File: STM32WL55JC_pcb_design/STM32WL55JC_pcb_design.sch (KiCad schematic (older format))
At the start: 27 parts

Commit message: Complete first version - todo: rf pins
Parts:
- removed J?: Conn_01x10_Male, Connector_JST:JST_GH_BM10B-GHS-TBT_1x10-1MP_P1.25mm_Vertical, symbol Connector:Conn_01x10_Male
- removed J?: Conn_01x07_Male, symbol Connector:Conn_01x07_Male
- added J?: Conn_02x02_Odd_Even, symbol Connector_Generic:Conn_02x02_Odd_Even
- added J?: Conn_01x06, symbol Connector_Generic:Conn_01x06
- added J?: Conn_02x05_Odd_Even, symbol Connector_Generic:Conn_02x05_Odd_Even
- added J?: Conn_01x13_Male, symbol Connector:Conn_01x13_Male
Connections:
- net labels added: 29V5, 5V, ADC_DO1, ADC_DO2, EXP_INT, EXP_SCL, EXP_SDA, NCS1_1, NCS1_2, NCS2_1, NCS2_2, NCS3_1, NCS3_2, NCS4_1, NCS4_2, NRST, OR1, OR2, OR3, OR4, PA0, PA1, PA7, PB0, PB1, PB10, PB11, PB6, PC0, PC1, PC4, PC5, PC6, SPI1_CLK, SPI2_CLK, SWCLK, SWDIO, SWO
- net labels removed: 29V, ADC1_CS, ADC2_CS, ADC_DOUT, ADC_SCLK, ENC1_1, ENC1_2, ENC1_3, ENC1_4, ENC2_1, ENC2_2, ENC2_3, ENC2_4, GND1, OR, Reset
- wire segments 151 -> 220
- no-connect marks 0 -> 2
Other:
- note added: "ST-Link Connector"
- note added: "Scintillator subsystem"

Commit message: Add temperature and humidty sensor, add rf connections
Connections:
- net labels added: PA8, RFI_N, RFI_P, RFO_HP, TempHumid_DRDY, VR_PA
- net labels removed: PB6, USB_RX, USB_TX
- wire segments 220 -> 227
- no-connect marks 2 -> 3
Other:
- moved on the sheet: J?
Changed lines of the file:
@@
 $Descr A4 11693 8268
 encoding utf-8
-Sheet 1 5
+Sheet 1 7
 Title ""
 Date ""
@@
 	1    0    0    -1
 $EndComp
-Text GLabel 8950 2400 2    50   Input ~ 0
+Text GLabel 8900 2400 2    50   Input ~ 0
 SPI1_CLK
 Wire Wire Line
@@
 	1    0    0    -1
 $EndComp
-$Sheet
-S 750  2100 750  1000
-U 612BE788
-F0 "Power Supply" 50
-F1 "Power supply.sch" 50
-F2 "3.3V" I R 1500 2300 50
-F3 "GND" I R 1500 2400 50
-F4 "USB_TX" I R 1500 2700 50
-F5 "USB_RX" I R 1500 2800 50
-F6 "29V5" I R 1500 2950 50
-F7 "5V" I R 1500 3050 50
-$EndSheet
 $Comp
 L power:+3.3V #PWR?
@@
 	1    0    0    -1
 $EndComp
-Text GLabel 3100 2350 2    50   Input ~ 0
+Text GLabel 3150 2450 2    50   Input ~ 0
 SCL
 Wire Wire Line
-	2950 2350 3100 2350
-$Sheet
-S 2150 2100 800  850
-U 61317136
-F0 "GPS and accelerometer" 50
-F1 "GPS_ACC.sch" 50
-F2 "SDA" I R 2950 2250 50
-F3 "SCL" I R 2950 2350 50
-F4 "TX" I R 2950 2500 50
-F5 "RX" I R 2950 2600 50
-$EndSheet
-Text GLabel 3100 2250 2    50   Input ~ 0
+	3000 2450 3150 2450
+Text GLabel 3150 2350 2    50   Input ~ 0
 SDA
 Wire Wire Line
-	2950 2250 3100 2250
+	3000 2350 3150 2350
 $Comp
 L STM32WL55JC_pcb_design-rescue:STM32WL55JCI7-MCU_ST_STM3255JCI7 U?
@@
 	1    0    0    -1
 $EndComp
-Text GLabel 3100 2600 2    50   Input ~ 0
+Text GLabel 3150 2700 2    50   Input ~ 0
 RX
 Wire Wire Line
-	2950 2600 3100 2600
-Wire Wire Line
-	2950 2500 3100 2500
-Text GLabel 3100 2500 2    50   Input ~ 0
+	3000 2700 3150 2700
+Wire Wire Line
+	3000 2600 3150 2600
+Text GLabel 3150 2600 2    50   Input ~ 0
 TX
 Wire Wire Line
-	1500 2700 1650 2700
-Wire Wire Line
-	1500 2800 1650 2800
-Text GLabel 1650 2800 2    50   Input ~ 0
-USB_RX
-Text GLabel 1650 2700 2    50   Input ~ 0
-USB_TX
-Wire Wire Line
 	4850 5000 4850 4900
 Wire Wire Line
-	4850 4900 4700 4900
-Wire Wire Line
-	4700 4900 4700 4950
+	4300 4900 4300 4950
 $Comp
 L power:GNDREF #PWR?
 U 1 1 61386153
-P 4700 4950
-F 0 "#PWR?" H 4700 4700 50  0001 C CNN
-F 1 "GNDREF" H 4705 4777 50  0000 C CNN
-F 2 "" H 4700 4950 50  0001 C CNN
-F 3 "" H 4700 4950 50  0001 C CNN
-	1    4700 4950
+P 4300 4950
+F 0 "#PWR?" H 4300 4700 50  0001 C CNN
+F 1 "GNDREF" H 4305 4777 50  0000 C CNN
+F 2 "" H 4300 4950 50  0001 C CNN
+F 3 "" H 4300 4950 50  0001 C CNN
+	1    4300 4950
 	1    0    0    -1
 $EndComp
@@
 	8750 3000 8900 3000
 Wire Wire Line
-	8750 2900 9000 2900
-Wire Wire Line
-	9000 2900 9000 2800
-Wire Wire Line
-	9350 2800 9350 2850
+	9250 2900 9250 2800
+Wire Wire Line
+	9600 2800 9600 2850
 $Comp
 L power:GNDREF #PWR?
 U 1 1 61439C4E
-P 9350 2850
-F 0 "#PWR?" H 9350 2600 50  0001 C CNN
-F 1 "GNDREF" H 9355 2677 50  0000 C CNN
-F 2 "" H 9350 2850 50  0001 C CNN
-F 3 "" H 9350 2850 50  0001 C CNN
-	1    9350 2850
-	1    0    0    -1
-$EndComp
-Wire Wire Line
-	9000 2800 9350 2800
+P 9600 2850
+F 0 "#PWR?" H 9600 2600 50  0001 C CNN
+F 1 "GNDREF" H 9605 2677 50  0000 C CNN
+F 2 "" H 9600 2850 50  0001 C CNN
+F 3 "" H 9600 2850 50  0001 C CNN
+	1    9600 2850
+	1    0    0    -1
+$EndComp
+Wire Wire Line
+	9250 2800 9600 2800
 $Comp
 L Device:C C?
@@
 Text GLabel 6850 900  1    50   Input ~ 0
 VDDPA
-Text GLabel 8950 2700 2    50   Input ~ 0
+Text GLabel 8900 2700 2    50   Input ~ 0
 VDDPA
 $Comp
@@
 Wire Wire Line
 	5200 3900 5350 3900
-Wire Wire Line
-	8750 2200 8950 2200
 $Comp
 L Connector_Generic:Conn_02x02_Odd_Even J?
 U 1 1 61363B01
-P 9150 2150
-F 0 "J?" H 9200 2367 50  0000 C CNN
-F 1 "Conn_02x02_Odd_Even" H 9200 2276 50  0000 C CNN
-F 2 "" H 9150 2150 50  0001 C CNN
-F 3 "~" H 9150 2150 50  0001 C CNN
-	1    9150 2150
-	1    0    0    -1
-$EndComp
-Wire Wire Line
-	8950 2200 8950 2150
-Wire Wire Line
-	8950 2200 8950 2250
-Connection ~ 8950 2200
-Wire Wire Line
-	9450 2150 9700 2150
-Wire Wire Line
-	9700 2150 9700 1950
+P 9500 2150
+F 0 "J?" H 9550 2367 50  0000 C CNN
+F 1 "Conn_02x02_Odd_Even" H 9550 2276 50  0000 C CNN
+F 2 "" H 9500 2150 50  0001 C CNN
+F 3 "~" H 9500 2150 50  0001 C CNN
+	1    9500 2150
+	1    0    0    -1
+$EndComp
+Wire Wire Line
+	9300 2200 9300 2150
+Wire Wire Line
+	9300 2200 9300 2250
+Connection ~ 9300 2200
+Wire Wire Line
+	9800 2150 10050 2150
+Wire Wire Line
+	10050 2150 10050 1950
 $Comp
 L power:+3.3V #PWR?
 U 1 1 6137A2D6
-P 9700 1950
-F 0 "#PWR?" H 9700 1800 50  0001 C CNN
-F 1 "+3.3V" H 9715 2123 50  0000 C CNN
-F 2 "" H 9700 1950 50  0001 C CNN
-F 3 "" H 9700 1950 50  0001 C CNN
-	1    9700 1950
-	1    0    0    -1
-$EndComp
-Wire Wire Line
-	9450 2250 9700 2250
-Wire Wire Line
-	9700 2250 9700 2450
+P 10050 1950
+F 0 "#PWR?" H 10050 1800 50  0001 C CNN
+F 1 "+3.3V" H 10065 2123 50  0000 C CNN
+F 2 "" H 10050 1950 50  0001 C CNN
+F 3 "" H 10050 1950 50  0001 C CNN
+	1    10050 1950
+	1    0    0    -1
+$EndComp
+Wire Wire Line
+	9800 2250 10050 2250
+Wire Wire Line
+	10050 2250 10050 2450
 $Comp
 L power:GNDREF #PWR?
 U 1 1 61383853
-P 9700 2450
-F 0 "#PWR?" H 9700 2200 50  0001 C CNN
-F 1 "GNDREF" H 9705 2277 50  0000 C CNN
-F 2 "" H 9700 2450 50  0001 C CNN
-F 3 "" H 9700 2450 50  0001 C CNN
-	1    9700 2450
-	1    0    0    -1
-$EndComp
-Wire Wire Line
-	1500 2950 1650 2950
-Wire Wire Line
-	1500 3050 1650 3050
-Text GLabel 1650 2950 2    50   Input ~ 0
+P 10050 2450
+F 0 "#PWR?" H 10050 2200 50  0001 C CNN
+F 1 "GNDREF" H 10055 2277 50  0000 C CNN
+F 2 "" H 10050 2450 50  0001 C CNN
+F 3 "" H 10050 2450 50  0001 C CNN
+	1    10050 2450
+	1    0    0    -1
+$EndComp
+Wire Wire Line
+	1500 2750 1650 2750
+Wire Wire Line
+	1500 2850 1650 2850
+Text GLabel 1650 2750 2    50   Input ~ 0
 29V5
-Text GLabel 1650 3050 2    50   Input ~ 0
+Text GLabel 1650 2850 2    50   Input ~ 0
 5V
 $Sheet
@@
 Text GLabel 5200 2800 0    50   Input ~ 0
 NCS1_1
-Wire Wire Line
-	8750 2500 8950 2500
 Text GLabel 5200 4900 0    50   Input ~ 0
 NCS1_2
@@
 Wire Wire Line
 	4850 5000 5350 5000
-Text GLabel 8950 2500 2    50   Input ~ 0
+Text GLabel 8900 2500 2    50   Input ~ 0
 NCS2_1
 Wire Wire Line
@@
 Text GLabel 5200 2100 0    50   Input ~ 0
 SWCLK
-Wire Wire Line
-	8950 2400 8750 2400
 Text GLabel 5200 3500 0    50   Input ~ 0
 SWO
@@
 	5350 5400 5200 5400
 Wire Wire Line
-	8750 2300 8950 2300
-Wire Wire Line
-	8750 2700 8950 2700
-Wire Wire Line
 	8750 3100 8900 3100
 Wire Wire Line
@@
 Text GLabel 5200 4700 0    50   Input ~ 0
 PA0
-Text GLabel 5200 5100 0    50   Input ~ 0
-PB6
 Text GLabel 10450 950  2    50   Input ~ 0
 PA0
-Text GLabel 10450 1450 2    50   Input ~ 0
-PB6
 Text GLabel 5200 5400 0    50   Input ~ 0
 PC5
@@
 Text GLabel 8900 4500 2    50   Input ~ 0
 PB0
-Text GLabel 10450 1250 2    50   Input ~ 0
+Text GLabel 10450 1350 2    50   Input ~ 0
 PB0
 Text GLabel 8900 4800 2    50   Input ~ 0
@@
 Text GLabel 8900 5300 2    50   Input ~ 0
 PB1
-Text GLabel 10450 1350 2    50   Input ~ 0
+Text GLabel 10450 1450 2    50   Input ~ 0
 PB1
 $Comp
@@
 	1    0    0    -1
 $EndComp
+$Sheet
+S 9800 5550 500  700
+U 613C9E7C
+F0 "LoRa" 50
+F1 "LoRa.sch" 50
+F2 "VR_PA" I R 10300 5650 50
+F3 "RFO_HP" I R 10300 5750 50
+F4 "RFI_P" I R 10300 5850 50
+F5 "RFI_N" I R 10300 5950 50
+$EndSheet
+Wire Wire Line
+	3000 2850 3150 2850
+Text GLabel 3150 2850 2    50   Input ~ 0
+TempHumid_DRDY
+$Sheet
+S 2200 2200 800  850
+U 61317136
+F0 "Sensors" 50
+F1 "Sensors.sch" 50
+F2 "SDA" I R 3000 2350 50
+F3 "SCL" I R 3000 2450 50
+F4 "TX" I R 3000 2600 50
+F5 "RX" I R 3000 2700 50
+F6 "TempHumid_DRDY" I R 3000 2850 50
+$EndSheet
+Text GLabel 5200 5100 0    50   Input ~ 0
+TempHumid_DRDY
+Wire Wire Line
+	4300 4900 4850 4900
+Wire Wire Line
+	10300 5650 10450 5650
+Wire Wire Line
+	10300 5750 10450 5750
+Wire Wire Line
+	10300 5850 10450 5850
+Wire Wire Line
+	10300 5950 10450 5950
+Text GLabel 10450 5650 2    50   Input ~ 0
+VR_PA
+Text GLabel 10450 5750 2    50   Input ~ 0
+RFO_HP
+Text GLabel 10450 5850 2    50   Input ~ 0
+RFI_P
+Text GLabel 10450 5950 2    50   Input ~ 0
+RFI_N
+Text GLabel 8900 1900 2    50   Input ~ 0
+RFO_HP
+NoConn ~ 8750 2000
+Text GLabel 8900 2600 2    50   Input ~ 0
+VR_PA
+Wire Wire Line
+	8750 2400 8900 2400
+Wire Wire Line
+	8750 2500 8900 2500
+Wire Wire Line
+	8750 2600 8900 2600
+Wire Wire Line
+	8750 2700 8900 2700
+Wire Wire Line
+	8750 2900 9250 2900
+Wire Wire Line
+	8750 2800 8900 2800
+Text GLabel 8900 2800 2    50   Input ~ 0
+RFI_N
+Wire Wire Line
+	8750 2200 9300 2200
+Wire Wire Line
+	8750 2300 8900 2300
+Text GLabel 8900 2300 2    50   Input ~ 0
+PA8
+Text GLabel 10450 1250 2    50   Input ~ 0
+PA8
+Text GLabel 8900 2100 2    50   Input ~ 0
+RFI_P
+Wire Wire Line
+	8750 1900 8900 1900
+Wire Wire Line
+	8750 2100 8900 2100
+$Sheet
+S 750  2100 750  950
+U 612BE788
+F0 "Power Supply" 50
+F1 "Power supply.sch" 50
+F2 "3.3V" I R 1500 2300 50
+F3 "GND" I R 1500 2400 50
+F4 "29V5" I R 1500 2750 50
+F5 "5V" I R 1500 2850 50
+$EndSheet
+$Sheet
+S 8800 5800 550  600
+U 616239B7
+F0 "USB_connection" 50
+F1 "USB_connection.sch" 50
+$EndSheet
 $EndSCHEMATC

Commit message: Add RTC
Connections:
- wire segments 227 -> 228
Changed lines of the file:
@@
 TempHumid_DRDY
 $Sheet
-S 2200 2200 800  850
+S 2200 2200 800  900
 U 61317136
-F0 "Sensors" 50
-F1 "Sensors.sch" 50
+F0 "Sensors + RTC" 50
+F1 "Sensors+RTC.sch" 50
 F2 "SDA" I R 3000 2350 50
 F3 "SCL" I R 3000 2450 50
@@
 F5 "RX" I R 3000 2700 50
 F6 "TempHumid_DRDY" I R 3000 2850 50
+F7 "5V" I R 3000 3000 50
 $EndSheet
 Text GLabel 5200 5100 0    50   Input ~ 0
@@
 F1 "USB_connection.sch" 50
 $EndSheet
+Wire Wire Line
+	3000 3000 3150 3000
+Text GLabel 3150 3000 2    50   Input ~ 0
+5V
 $EndSCHEMATC

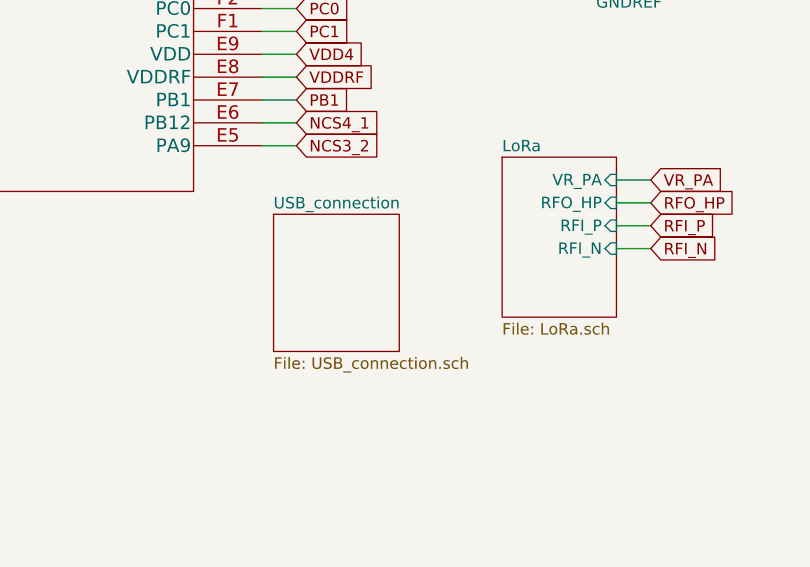
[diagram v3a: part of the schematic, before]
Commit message: Finish RF matching network
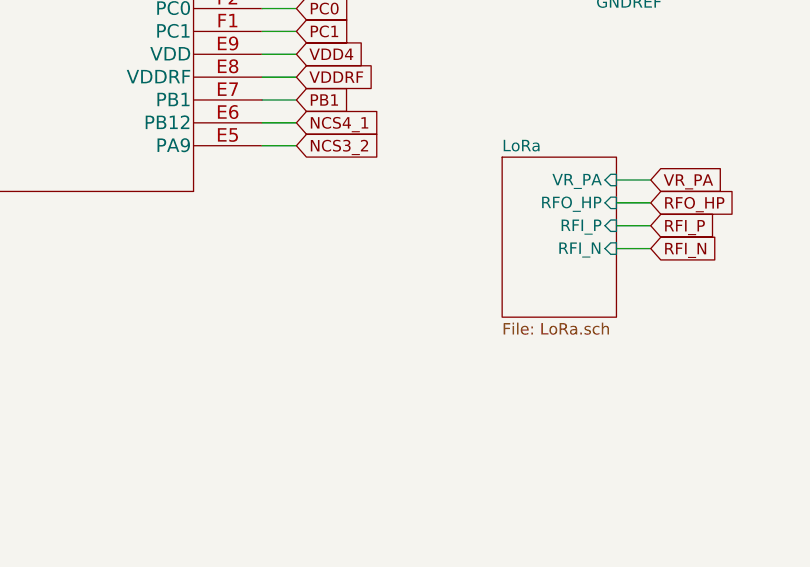
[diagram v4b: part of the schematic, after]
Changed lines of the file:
@@
 $Descr A4 11693 8268
 encoding utf-8
-Sheet 1 7
+Sheet 1 6
 Title ""
 Date ""
@@
 F5 "5V" I R 1500 2850 50
 $EndSheet
-$Sheet
-S 8800 5800 550  600
-U 616239B7
-F0 "USB_connection" 50
-F1 "USB_connection.sch" 50
-$EndSheet
-Wire Wire Line
+Wire Wire Line

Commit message: Update ADC section to work with MAX11635
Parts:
- removed J?: Conn_01x06, symbol Connector_Generic:Conn_01x06
- removed J?: Conn_01x13_Male, symbol Connector:Conn_01x13_Male
- added J?: Conn_01x01_Male, symbol Connector:Conn_01x01_Male
- added J? (x4): Conn_01x04, symbol Connector_Generic:Conn_01x04
- added J? (x4): Conn_01x07, symbol Connector_Generic:Conn_01x07
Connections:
- net labels added: ADC_CNVST1_1, ADC_CNVST1_2, ADC_CNVST2_1, ADC_CNVST2_2, ADC_CNVST3_1, ADC_CNVST3_2, ADC_CNVST4_1, ADC_CNVST4_2, ADC_CS1_1, ADC_CS1_2, ADC_CS2_1, ADC_CS2_2, ADC_CS3_1, ADC_CS3_2, ADC_CS4_1, ADC_CS4_2, ADC_DIN1, ADC_DIN2, ADC_DOUT1, ADC_DOUT2, ADC_SCLK1, ADC_SCLK2, RF_CTRL
- net labels removed: PA0, PA1, PA7, PA8, PB0, PB1, PB10, PB11, PC0, PC1, PC4, PC6
- wire segments 228 -> 235
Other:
- moved on the sheet: C?, J?, L?, U?, Y?

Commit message: Finish component selection and footprint assignment
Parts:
- removed J? (x4): Conn_01x04, symbol Connector_Generic:Conn_01x04
- removed J? (x4): Conn_01x07, symbol Connector_Generic:Conn_01x07
- removed Y?: 32MHz, symbol Device:Crystal
- added C46, C53: 8pF, Capacitor_SMD:C_0805_2012Metric, symbol Device:C_Small
- added C47, C49: 15pF, Capacitor_SMD:C_0805_2012Metric, symbol Device:C_Small
- added J1, J2, J4, J7: Conn_01x03, Connector_JST:JST_GH_BM03B-GHS-TBT_1x03-1MP_P1.25mm_Vertical, symbol Connector_Generic:Conn_01x03
- added J5, J6, J8, J9: Conn_01x09, Connector_JST:JST_GH_BM09B-GHS-TBT_1x09-1MP_P1.25mm_Vertical, symbol Connector_Generic:Conn_01x09
- added Y1: 32MHz, Oscillator:Oscillator_SMD_SeikoEpson_SG210-4Pin_2.5x2.0mm, symbol Device:Crystal_GND24
- C1, C10, C11, C12, C13, C14, C15, C16, C17, C18, C19, C2, C20, C21, C3, C4, C5, C6, C7, C8, C9: renamed from C?; footprint (none) -> Capacitor_SMD:C_0805_2012Metric
- J10: renamed from J?; footprint (none) -> Connector_PinHeader_2.54mm:PinHeader_1x01_P2.54mm_Vertical
- J11: renamed from J?; footprint (none) -> Connector_PinHeader_2.54mm:PinHeader_2x02_P2.54mm_Vertical_SMD
- J3: renamed from J?; footprint (none) -> Connector_PinHeader_1.27mm:PinHeader_2x05_P1.27mm_Vertical_SMD
- L1: renamed from L?; footprint (none) -> Inductor_SMD:L_0805_2012Metric
- U1: renamed from U?; footprint UFBGA_L55JCI7_STM -> MCU_ST_STM3255JCI7:STM32WL55JCI7
- Y2: renamed from Y?; footprint (none) -> SC20S-12.5PF20PPM:SC20S125PF20PPM
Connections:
- net +3V3: now also J1.2 (Pin_2), J2.2 (Pin_2), J4.2 (Pin_2), J7.2 (Pin_2)
- net 5V: now also J1.3 (Pin_3), J2.3 (Pin_3), J4.3 (Pin_3), J7.3 (Pin_3)
- net ADC_CNVST1_1: now also J5.4 (Pin_4)
- net ADC_CNVST1_2: now also J5.1 (Pin_1)
- net ADC_CNVST2_1: now also J6.4 (Pin_4)
- net ADC_CNVST2_2: now also J6.1 (Pin_1)
- net ADC_CNVST3_1: now also J8.4 (Pin_4)
- net ADC_CNVST3_2: now also J8.1 (Pin_1)
- net ADC_CNVST4_1: now also J9.4 (Pin_4)
- net ADC_CNVST4_2: now also J9.1 (Pin_1)
- net ADC_CS1_1: now also J5.5 (Pin_5)
- net ADC_CS1_2: now also J5.2 (Pin_2)
- net ADC_CS2_1: now also J6.5 (Pin_5)
- net ADC_CS2_2: now also J6.2 (Pin_2)
- net ADC_CS3_1: now also J8.5 (Pin_5)
- net ADC_CS3_2: now also J8.2 (Pin_2)
- net ADC_CS4_1: now also J9.5 (Pin_5)
- net ADC_CS4_2: now also J9.2 (Pin_2)
- net ADC_DIN1: now also J5.7 (Pin_7), J6.7 (Pin_7)
- net ADC_DIN2: now also J8.7 (Pin_7), J9.7 (Pin_7)
- net ADC_DOUT1: now also J5.8 (Pin_8), J6.8 (Pin_8)
- net ADC_DOUT2: now also J8.8 (Pin_8), J9.8 (Pin_8)
- net ADC_SCLK1: now also J5.6 (Pin_6), J6.6 (Pin_6)
- net ADC_SCLK2: now also J8.6 (Pin_6), J9.6 (Pin_6)
- net GNDREF: now also C46.2, C47.2, C49.2, C53.2, J1.1 (Pin_1), J2.1 (Pin_1), J4.1 (Pin_1), J7.1 (Pin_1), Y1.2, Y1.4; no longer U1.B6 (PC14-_OSC32_IN), U1.C5 (PC15-_OSC32__OUT), U1.F8 (OSC_OUT), U1.G9 (OSC_IN), Y2.1, Y2.2
- net OR2: now also U1.D4 (PC2); no longer U1.D6 (PA0)
- net OR3: now also U1.D6 (PA0); no longer U1.D4 (PC2)
- new net ADC_EOC1_1: J5.9 (Pin_9)
- new net ADC_EOC1_2: J5.3 (Pin_3)
- new net ADC_EOC2_1: J6.9 (Pin_9)
- new net ADC_EOC2_2: J6.3 (Pin_3)
- new net ADC_EOC3_1: J8.9 (Pin_9)
- new net ADC_EOC3_2: J8.3 (Pin_3)
- new net ADC_EOC4_1: J9.9 (Pin_9)
- new net ADC_EOC4_2: J9.3 (Pin_3)
- new net OSC32_IN: C47.1, U1.B6 (PC14-_OSC32_IN), Y2.1
- new net OSC32_OUT: C49.1, U1.C5 (PC15-_OSC32__OUT), Y2.2
- new net OSC_IN: C46.1, U1.G9 (OSC_IN), Y1.1
- new net OSC_OUT: C53.1, U1.F8 (OSC_OUT), Y1.3
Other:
- note added: "External clocks"
- note added: "GPIO\n"
- moved on the sheet: J10, Y2
